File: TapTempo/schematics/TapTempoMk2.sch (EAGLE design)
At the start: 70 parts, among them IC1 TLV1117-33CDCY, IC3 TL072D, IC4 LM4040B10, Q1 BC846, Q3 BC846, Q301 BC846, Q701 BC846, U1 STM32F100CBT6B, X2 53048-05, Y2 8MHz

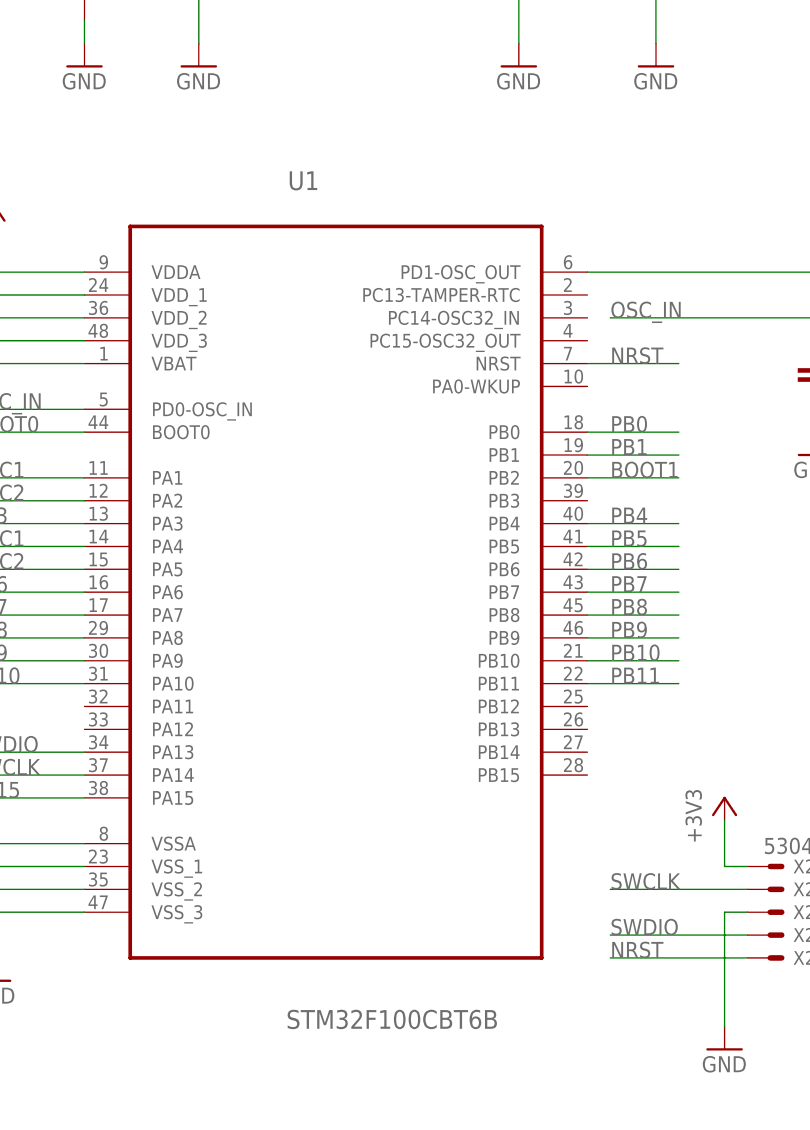
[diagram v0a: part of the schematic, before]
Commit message: changed to Rebel.lbr caps and resistors
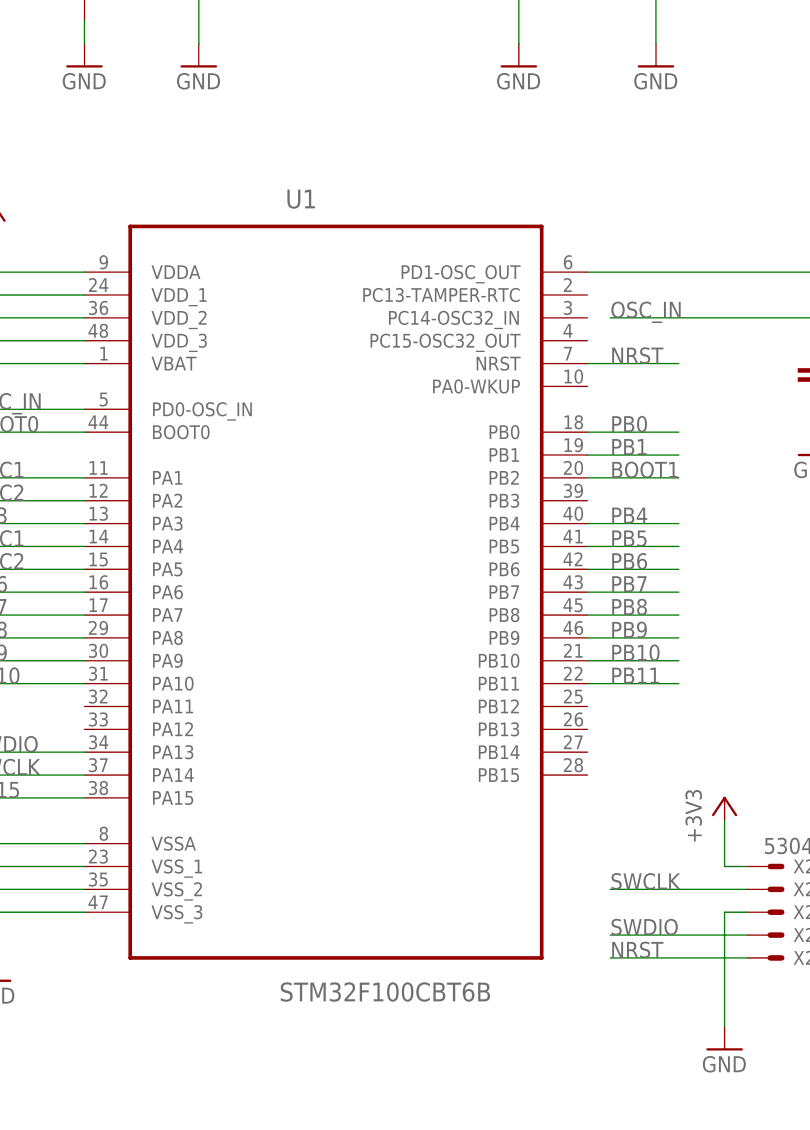
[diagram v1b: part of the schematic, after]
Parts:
- C1, C10, C100, C11, C15, C2, C3, C4, C5, C6, C7, C8, C804: device resistor:C-EUC0603 -> Rebel:C-EUC0603
- R1, R10, R101, R11, R4, R401, R402, R403, R404, R5, R501, R502, R504, R6, R601, R602, R603, R7, R701, R702, R703, R8, R9: device resistor:R-EU_R0603 -> Rebel:R-EU_0603

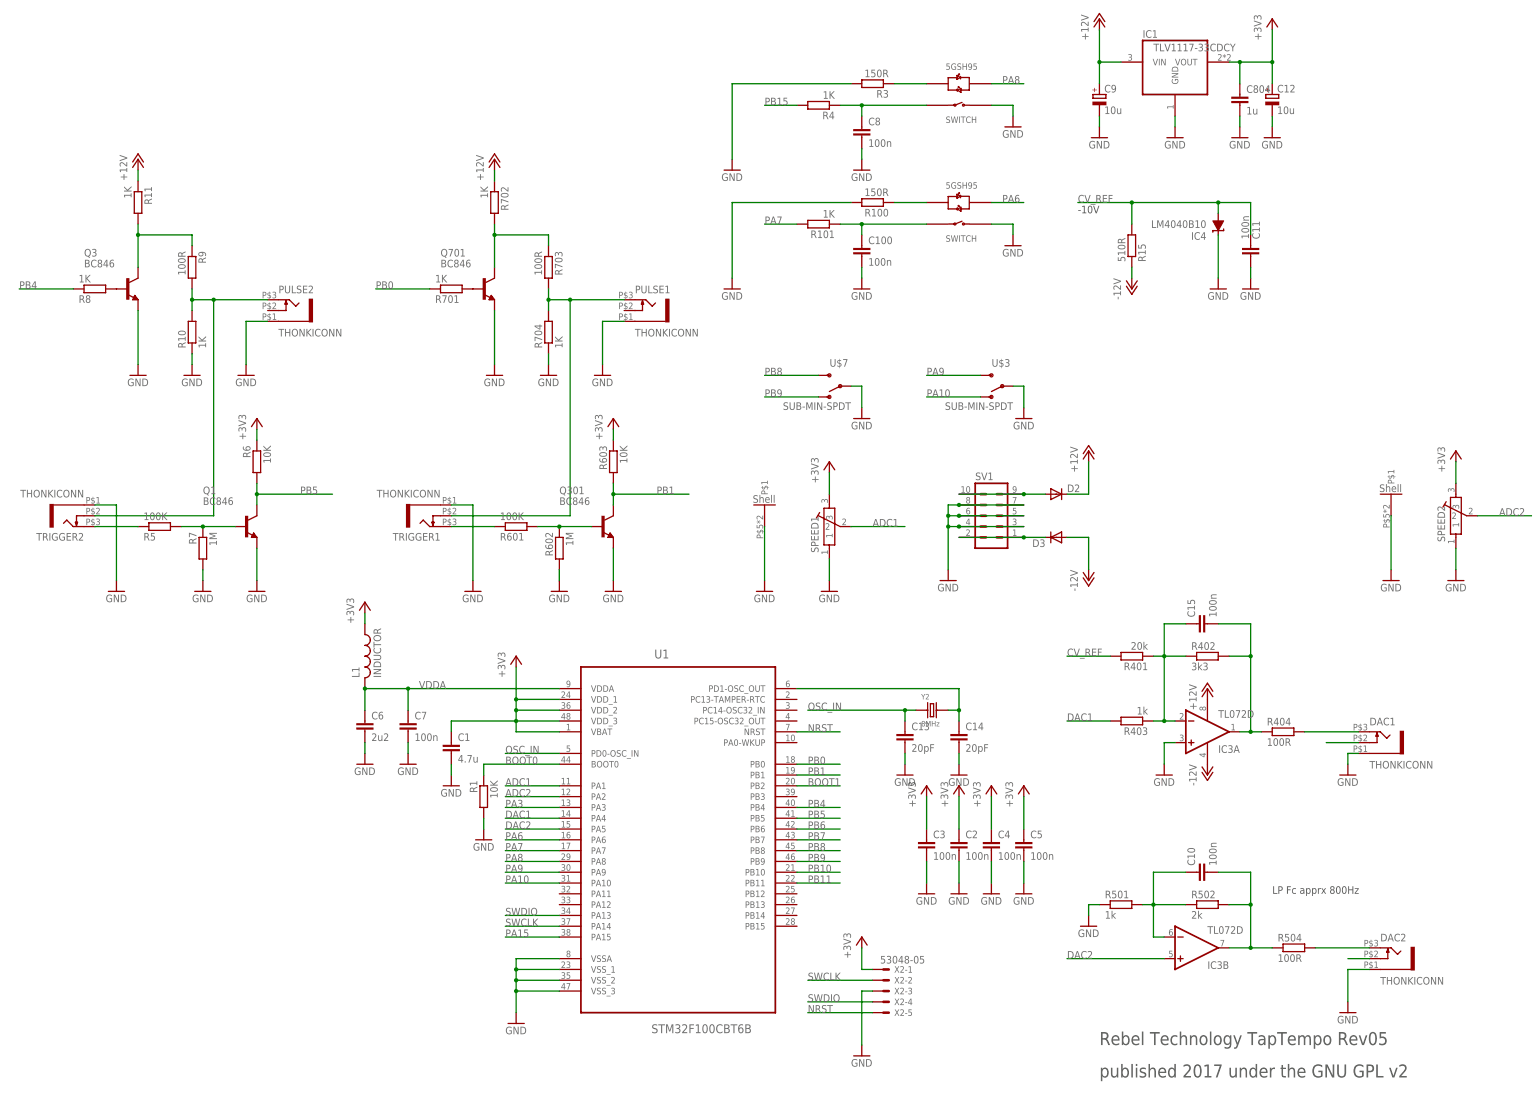
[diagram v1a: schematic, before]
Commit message: renumbered parts
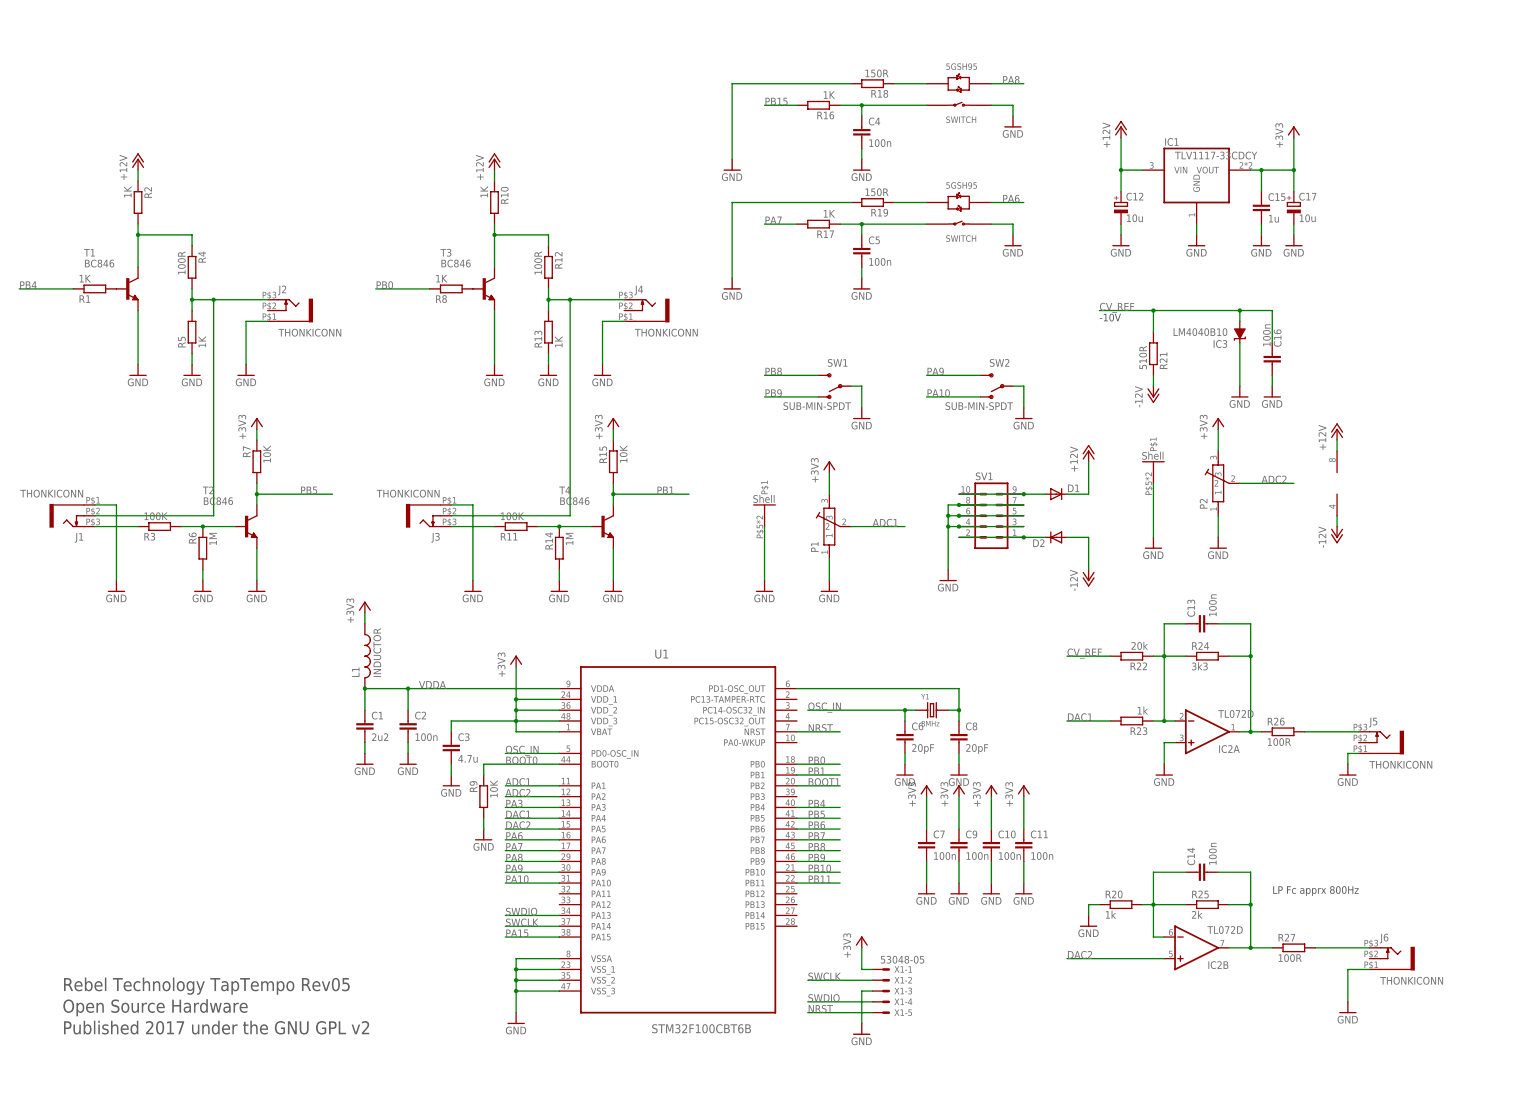
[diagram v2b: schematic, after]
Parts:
- removed C100: 100n, Rebel:C-EUC0603
- removed C804: 1u, Rebel:C-EUC0603
- removed D3: (no value), SparkFun:DIODESMA
- removed IC4: LM4040B10, texas:LM4041C12DBZ
- removed R601: 100K, Rebel:R-EU_0603
- removed R603: 10K, Rebel:R-EU_0603
- removed R701, R702: 1K, Rebel:R-EU_0603
- removed SPEED2: POT-ALPS-RK09L1140, Rebel:POT-ALPS-RK09L1140
- added C16: 100n, Rebel:C-EUC0603
- added C17: 10u, resistor:CPOL-EUA
- added D1: (no value), SparkFun:DIODESMA
- added IC2: TL072D, linear:TL072D
- added P2: POT-ALPS-RK09L1140, Rebel:POT-ALPS-RK09L1140
- added R16, R2: 1K, Rebel:R-EU_0603
- added R18: 150R, Rebel:R-EU_0603
- added R21: 510R, Rebel:R-EU_0603
- C1: value 4.7u -> 2u2
- C13, C14: value 20pF -> 100n
- C15: value 100n -> 1u
- C3: value 100n -> 4.7u
- C6: value 2u2 -> 20pF
- C8: value 100n -> 20pF
- C9: value 10u -> 100n; device resistor:CPOL-EUA -> Rebel:C-EUC0603; FARNELL 882-3014 -> (none)
- IC3: value TL072D -> LM4040B10; device linear:TL072D -> texas:LM4041C12DBZ
- R1: value 10K -> 1K
- R11: value 1K -> 100K
- R15: value 510R -> 10K
- R3: value 150R -> 100K
- R4: value 1K -> 100R
- R5: value 100K -> 1K
- R6: value 10K -> 1M
- R7: value 1M -> 10K
- R9: value 100R -> 10K
- renumbered B1 to PB2, B2 to PB1, DAC1 to J5, DAC2 to J6, PULSE1 to J4, PULSE2 to J2, Q1 to T2, Q3 to T1, Q301 to T4, Q701 to T3, R100 to R19, R101 to R17, R401 to R22, R402 to R24, R403 to R23, R404 to R26, R501 to R20, R502 to R25, R504 to R27, R602 to R14, R703 to R12, R704 to R13, SPEED1 to P1, TRIGGER1 to J3, TRIGGER2 to J1, U$3 to SW2, U$7 to SW1, X2 to X1, Y2 to Y1
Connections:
- removed net N$29: J6.4
- removed net N$8: J5.4
- net +12V: now also C12.+, D1.C, IC2P.V+, R10.1, R2.1; no longer C9.+, D2.C, IC3P.V+, R11.1, R702.1
- net +3V3: now also C10.1, C11.1, C15.1, C17.+, C7.1, C9.1, P2G$1.3, R15.1, R7.1; no longer C1.1, C12.+, C2.1, C4.1, C5.1, C804.1, R6.1, R603.1, SPEED2G$1.3
- net -12V: now also D2.A, IC2P.V-, R21.1; no longer D3.A, IC3P.V-, R15.1
- net ADC2: now also P2G$1.2; no longer SPEED2G$1.2
- net BOOT0: now also R9.1; no longer R1.1
- net CV_REF: now also C16.1, IC3.A, R21.2; no longer C11.1, IC4.A, R15.2
- net DAC2: now also IC2B.+IN; no longer IC3B.+IN
- net GND: now also C10.2, C15.2, C16.2, C17.-, C9.2, IC2A.+IN, IC3.C, P2G$1.1, P2G$2.P$1, R18.2, R5.1, R6.2, R9.2; no longer C100.2, C13.2, C14.2, C804.2, C9.-, IC3A.+IN, IC4.C, R1.2, R10.1, R3.2, R7.2, SPEED2G$1.1, SPEED2G$2.P$1
- net N$1: now also C8.1; no longer C14.1
- net N$10: now also R3.2, R6.1; no longer R5.2, R7.1
- net N$11: now also R1.2; no longer R8.2
- net N$12: now also R2.2, R4.1; no longer R11.2, R9.1
- net N$13: now also C13.1, IC2A.-IN; no longer C15.1, IC3A.-IN
- net N$14: now also R3.1; no longer R5.1
- net N$15: now also R4.2, R5.2; no longer R10.2, R9.2
- net N$16: now also D2.C; no longer D3.C
- net N$17: now also C5.1; no longer C100.1
- net N$18: now also C4.1, R16.1; no longer C8.1, R4.1
- net N$23: now also R11.1; no longer R601.1
- net N$27: now also R11.2; no longer R601.2
- net N$3: now also C14.2, IC2B.OUT; no longer C10.2, IC3B.OUT
- net N$34: now also R8.2; no longer R701.2
- net N$38: now also R10.2; no longer R702.2
- net N$4: now also C14.1, IC2B.-IN; no longer C10.1, IC3B.-IN
- net N$6: now also D1.A; no longer D2.A
- net N$7: now also C13.2, IC2A.OUT; no longer C15.2, IC3A.OUT
- net N$9: now also R18.1; no longer R3.1
- net OSC_IN: now also C6.1; no longer C13.1
- net PB0: now also R8.1; no longer R701.1
- net PB1: now also R15.2; no longer R603.2
- net PB15: now also R16.2; no longer R4.2
- net PB4: now also R1.1; no longer R8.1
- net PB5: now also R7.2; no longer R6.2
- net VDDA: now also C1.1, C2.1; no longer C6.1, C7.1
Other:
- note added: "Open Source Hardware"
- note added: "Published 2017 under the GNU GPL v2"
- note removed: "published 2017 under the GNU GPL v2"
- moved on the sheet: C1, C10, C11, C12, C13, C14, C15, C2, C3, C4, C5, C6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

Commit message: arranged labels
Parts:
- added C18, C19: 100n, Rebel:C-EUC0603
- R13: device resistor:R-EU_R0603 -> Rebel:R-EU_0603
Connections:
- net +12V: now also C19.1
- net -12V: now also C18.1
- net GND: now also C18.2, C19.2
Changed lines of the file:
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@@
 <part name="R8" library="Rebel" deviceset="R-EU_" device="0603" value="1K"/>
 <part name="R12" library="Rebel" deviceset="R-EU_" device="0603" value="100R"/>
-<part name="R13" library="resistor" deviceset="R-EU_" device="R0603" value="1K"/>
+<part name="R13" library="Rebel" deviceset="R-EU_" device="0603" value="1K"/>
 <part name="GND14" library="supply1" deviceset="GND" device=""/>
 <part name="GND16" library="supply1" deviceset="GND" device=""/>
@@
 <part name="SV1" library="con-lstb" deviceset="MA05-2" device=""/>
 <part name="C13" library="Rebel" deviceset="C-EU" device="C0603" value="100n"/>
+<part name="C18" library="Rebel" deviceset="C-EU" device="C0603" value="100n"/>
+<part name="C19" library="Rebel" deviceset="C-EU" device="C0603" value="100n"/>
+<part name="GND48" library="supply1" deviceset="GND" device=""/>
 </parts>
 <sheets>
@@
 <instance part="IC2" gate="B" x="152.4" y="-2.54" rot="MR180"/>
 <instance part="IC2" gate="P" x="185.42" y="106.68"/>
-<instance part="P-3" gate="1" x="185.42" y="93.98"/>
-<instance part="P+5" gate="1" x="185.42" y="119.38"/>
+<instance part="P-3" gate="1" x="185.42" y="91.44"/>
+<instance part="P+5" gate="1" x="185.42" y="121.92"/>
 <instance part="C3" gate="G$1" x="-22.86" y="45.72"/>
 <instance part="C9" gate="G$1" x="96.52" y="22.86"/>
@@
 <instance part="SV1" gate="G$1" x="104.14" y="99.06"/>
 <instance part="C13" gate="G$1" x="152.4" y="73.66" rot="R90"/>
+<instance part="C18" gate="G$1" x="190.5" y="96.52" rot="R90"/>
+<instance part="C19" gate="G$1" x="190.5" y="116.84" rot="R90"/>
+<instance part="GND48" gate="1" x="198.12" y="91.44"/>
 </instances>
 <busses>
@@
 <pinref part="P+5" gate="1" pin="+12V"/>
 <wire x1="185.42" y1="114.3" x2="185.42" y2="116.84" width="0.1524" layer="91"/>
+<pinref part="C19" gate="G$1" pin="1"/>
+<wire x1="185.42" y1="116.84" x2="185.42" y2="119.38" width="0.1524" layer="91"/>
+<wire x1="187.96" y1="116.84" x2="185.42" y2="116.84" width="0.1524" layer="91"/>
+<junction x="185.42" y="116.84"/>
 </segment>
 <segment>
@@
 <junction x="96.52" y="101.6"/>
 </segment>
+<segment>
+<pinref part="C19" gate="G$1" pin="2"/>
+<pinref part="GND48" gate="1" pin="GND"/>
+<wire x1="195.58" y1="116.84" x2="198.12" y2="116.84" width="0.1524" layer="91"/>
+<wire x1="198.12" y1="116.84" x2="198.12" y2="96.52" width="0.1524" layer="91"/>
+<pinref part="C18" gate="G$1" pin="2"/>
+<wire x1="198.12" y1="96.52" x2="198.12" y2="93.98" width="0.1524" layer="91"/>
+<wire x1="198.12" y1="96.52" x2="195.58" y2="96.52" width="0.1524" layer="91"/>
+<junction x="198.12" y="96.52"/>
+</segment>
 </net>
 <net name="-12V" class="0">
@@
 <pinref part="P-3" gate="1" pin="-12V"/>
 <wire x1="185.42" y1="99.06" x2="185.42" y2="96.52" width="0.1524" layer="91"/>
-</segment>
-<segment>
+<pinref part="C18" gate="G$1" pin="1"/>
+<wire x1="185.42" y1="96.52" x2="185.42" y2="93.98" width="0.1524" layer="91"/>
+<wire x1="187.96" y1="96.52" x2="185.42" y2="96.52" width="0.1524" layer="91"/>
+<junction x="185.42" y="96.52"/>
+</segment>
+<segment>

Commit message: draft cube firmware for Chronos mk2
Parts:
- renumbered J1 to TEMPO2, J2 to TR2, J3 to TEMPO1, J4 to TR1, J5 to DAC1, J6 to DAC2, PB1 to PUSH2, PB2 to PUSH1
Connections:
- net PA10 renamed SW2B
- net PA6 renamed LED1
- net PA7 renamed PUSH1
- net PA8 renamed LED2
- net PA9 renamed SW2A
- net PB0 renamed TR1
- net PB1 renamed TEMPO1
- net PB4 renamed TR2
- net PB5 renamed TEMPO2
- net PB8 renamed SW1A
- net PB9 renamed SW1B
- removed net PA15: U1.PA15
- removed net PA3: U1.PA3
- removed net PB10: U1.PB10
- removed net PB11: U1.PB11
- removed net PB15: R16.2
- removed net PB6: U1.PB6
- removed net PB7: U1.PB7
- new net PUSH2: R16.2, U1.PB15
